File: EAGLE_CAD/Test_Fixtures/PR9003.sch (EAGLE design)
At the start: 2 parts, among them J1 AVR_SPI_PRG_6NS, J2 AVR_SPI_PRG_6NS

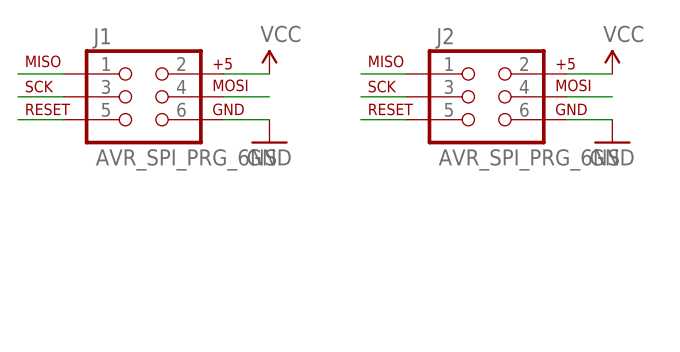
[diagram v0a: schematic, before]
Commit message: PR9003
Added external vcc line to programmer pcb
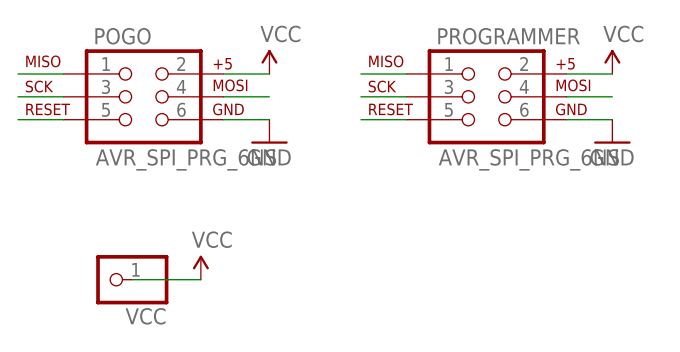
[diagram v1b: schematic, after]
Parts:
- added VCC: (no value), adafruit:PINHD-1X1
- renumbered J1 to POGO, J2 to PROGRAMMER
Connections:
- net VCC: now also VCC.1
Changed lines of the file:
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@@
 </classes>
 <parts>
-<part name="J1" library="SparkFun-Connectors" deviceset="AVR_SPI_PRG_6" device="NS"/>
-<part name="J2" library="SparkFun-Connectors" deviceset="AVR_SPI_PRG_6" device="NS"/>
+<part name="POGO" library="SparkFun-Connectors" deviceset="AVR_SPI_PRG_6" device="NS"/>
+<part name="PROGRAMMER" library="SparkFun-Connectors" deviceset="AVR_SPI_PRG_6" device="NS"/>
 <part name="GND1" library="SparkFun-Aesthetics" deviceset="GND" device=""/>
 <part name="GND2" library="SparkFun-Aesthetics" deviceset="GND" device=""/>
 <part name="SUPPLY1" library="SparkFun-Aesthetics" deviceset="VCC" device=""/>
 <part name="SUPPLY2" library="SparkFun-Aesthetics" deviceset="VCC" device=""/>
+<part name="VCC" library="adafruit" deviceset="PINHD-1X1" device=""/>
+<part name="SUPPLY3" library="SparkFun-Aesthetics" deviceset="VCC" device=""/>
 </parts>
 <sheets>
@@
 </plain>
 <instances>
-<instance part="J1" gate="G$1" x="20.32" y="17.78"/>
-<instance part="J2" gate="G$1" x="58.42" y="17.78"/>
+<instance part="POGO" gate="G$1" x="20.32" y="17.78"/>
+<instance part="PROGRAMMER" gate="G$1" x="58.42" y="17.78"/>
 <instance part="GND1" gate="1" x="35.56" y="12.7"/>
 <instance part="GND2" gate="1" x="73.66" y="12.7"/>
 <instance part="SUPPLY1" gate="G$1" x="35.56" y="20.32"/>
 <instance part="SUPPLY2" gate="G$1" x="73.66" y="20.32"/>
+<instance part="VCC" gate="G$1" x="17.78" y="-2.54" rot="R180"/>
+<instance part="SUPPLY3" gate="G$1" x="27.94" y="-2.54"/>
 </instances>
 <busses>
@@
 <net name="MISO" class="0">
 <segment>
-<pinref part="J1" gate="G$1" pin="1"/>
+<pinref part="POGO" gate="G$1" pin="1"/>
 <wire x1="12.7" y1="20.32" x2="7.62" y2="20.32" width="0.1524" layer="91"/>
 </segment>
 <segment>
-<pinref part="J2" gate="G$1" pin="1"/>
+<pinref part="PROGRAMMER" gate="G$1" pin="1"/>
 <wire x1="50.8" y1="20.32" x2="45.72" y2="20.32" width="0.1524" layer="91"/>
 </segment>
@@
 <net name="SCK" class="0">
 <segment>
-<pinref part="J1" gate="G$1" pin="3"/>
+<pinref part="POGO" gate="G$1" pin="3"/>
 <wire x1="12.7" y1="17.78" x2="7.62" y2="17.78" width="0.1524" layer="91"/>
 </segment>
 <segment>
-<pinref part="J2" gate="G$1" pin="3"/>
+<pinref part="PROGRAMMER" gate="G$1" pin="3"/>
 <wire x1="50.8" y1="17.78" x2="45.72" y2="17.78" width="0.1524" layer="91"/>
 </segment>
@@
 <net name="RESET" class="0">
 <segment>
-<pinref part="J1" gate="G$1" pin="5"/>
+<pinref part="POGO" gate="G$1" pin="5"/>
 <wire x1="12.7" y1="15.24" x2="7.62" y2="15.24" width="0.1524" layer="91"/>
 </segment>
 <segment>
-<pinref part="J2" gate="G$1" pin="5"/>
+<pinref part="PROGRAMMER" gate="G$1" pin="5"/>
 <wire x1="50.8" y1="15.24" x2="45.72" y2="15.24" width="0.1524" layer="91"/>
 </segment>
@@
 <net name="MOSI" class="0">
 <segment>
-<pinref part="J1" gate="G$1" pin="4"/>
+<pinref part="POGO" gate="G$1" pin="4"/>
 <wire x1="30.48" y1="17.78" x2="35.56" y2="17.78" width="0.1524" layer="91"/>
 </segment>
 <segment>
-<pinref part="J2" gate="G$1" pin="4"/>
+<pinref part="PROGRAMMER" gate="G$1" pin="4"/>
 <wire x1="68.58" y1="17.78" x2="73.66" y2="17.78" width="0.1524" layer="91"/>
 </segment>
@@
 <net name="GND" class="0">
 <segment>
-<pinref part="J1" gate="G$1" pin="6"/>
+<pinref part="POGO" gate="G$1" pin="6"/>
 <wire x1="30.48" y1="15.24" x2="35.56" y2="15.24" width="0.1524" layer="91"/>
 <pinref part="GND1" gate="1" pin="GND"/>
 </segment>
 <segment>
-<pinref part="J2" gate="G$1" pin="6"/>
+<pinref part="PROGRAMMER" gate="G$1" pin="6"/>
 <wire x1="68.58" y1="15.24" x2="73.66" y2="15.24" width="0.1524" layer="91"/>
 <pinref part="GND2" gate="1" pin="GND"/>
@@
 <net name="VCC" class="0">
 <segment>
-<pinref part="J1" gate="G$1" pin="2"/>
+<pinref part="POGO" gate="G$1" pin="2"/>
 <wire x1="30.48" y1="20.32" x2="35.56" y2="20.32" width="0.1524" layer="91"/>
 <pinref part="SUPPLY1" gate="G$1" pin="VCC"/>
 </segment>
 <segment>
-<pinref part="J2" gate="G$1" pin="2"/>
+<pinref part="PROGRAMMER" gate="G$1" pin="2"/>
 <wire x1="68.58" y1="20.32" x2="73.66" y2="20.32" width="0.1524" layer="91"/>
 <pinref part="SUPPLY2" gate="G$1" pin="VCC"/>
 </segment>
+<segment>
+<pinref part="VCC" gate="G$1" pin="1"/>
+<pinref part="SUPPLY3" gate="G$1" pin="VCC"/>
+<wire x1="27.94" y1="-2.54" x2="20.32" y2="-2.54" width="0.1524" layer="91"/>
+</segment>
 </net>

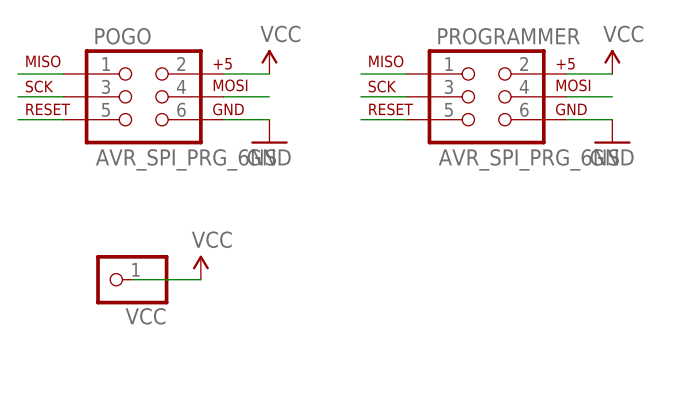
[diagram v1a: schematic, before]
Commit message: PR9003
Updated programmer w/ external vcc & gnd
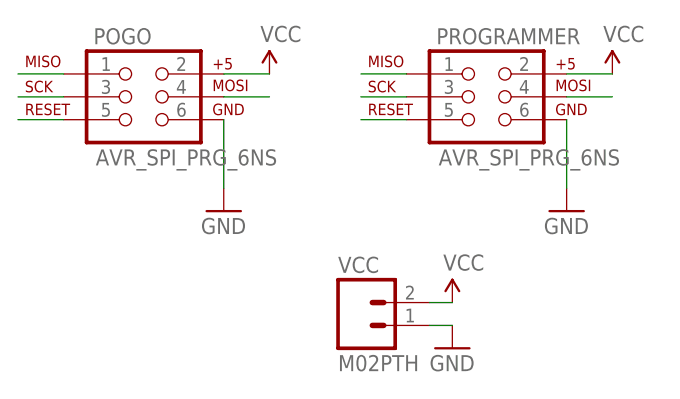
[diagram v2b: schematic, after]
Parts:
- VCC: value (none) -> M02PTH; device adafruit:PINHD-1X1 -> SparkFun-Connectors:M02PTH
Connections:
- net GND: now also VCC.1
- net VCC: now also VCC.2; no longer VCC.1
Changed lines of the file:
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@@
 <part name="SUPPLY1" library="SparkFun-Aesthetics" deviceset="VCC" device=""/>
 <part name="SUPPLY2" library="SparkFun-Aesthetics" deviceset="VCC" device=""/>
-<part name="VCC" library="adafruit" deviceset="PINHD-1X1" device=""/>
 <part name="SUPPLY3" library="SparkFun-Aesthetics" deviceset="VCC" device=""/>
+<part name="VCC" library="SparkFun-Connectors" deviceset="M02" device="PTH"/>
+<part name="GND3" library="SparkFun-Aesthetics" deviceset="GND" device=""/>
 </parts>
 <sheets>
@@
 <instance part="POGO" gate="G$1" x="20.32" y="17.78"/>
 <instance part="PROGRAMMER" gate="G$1" x="58.42" y="17.78"/>
-<instance part="GND1" gate="1" x="35.56" y="12.7"/>
-<instance part="GND2" gate="1" x="73.66" y="12.7"/>
+<instance part="GND1" gate="1" x="30.48" y="5.08"/>
+<instance part="GND2" gate="1" x="68.58" y="5.08"/>
 <instance part="SUPPLY1" gate="G$1" x="35.56" y="20.32"/>
 <instance part="SUPPLY2" gate="G$1" x="73.66" y="20.32"/>
-<instance part="VCC" gate="G$1" x="17.78" y="-2.54" rot="R180"/>
-<instance part="SUPPLY3" gate="G$1" x="27.94" y="-2.54"/>
+<instance part="SUPPLY3" gate="G$1" x="55.88" y="-5.08"/>
+<instance part="VCC" gate="G$1" x="45.72" y="-7.62"/>
+<instance part="GND3" gate="1" x="55.88" y="-10.16"/>
 </instances>
 <busses>
@@
 <segment>
 <pinref part="POGO" gate="G$1" pin="6"/>
-<wire x1="30.48" y1="15.24" x2="35.56" y2="15.24" width="0.1524" layer="91"/>
+<wire x1="30.48" y1="15.24" x2="30.48" y2="7.62" width="0.1524" layer="91"/>
 <pinref part="GND1" gate="1" pin="GND"/>
 </segment>
 <segment>
 <pinref part="PROGRAMMER" gate="G$1" pin="6"/>
-<wire x1="68.58" y1="15.24" x2="73.66" y2="15.24" width="0.1524" layer="91"/>
+<wire x1="68.58" y1="15.24" x2="68.58" y2="7.62" width="0.1524" layer="91"/>
 <pinref part="GND2" gate="1" pin="GND"/>
+</segment>
+<segment>
+<pinref part="VCC" gate="G$1" pin="1"/>
+<pinref part="GND3" gate="1" pin="GND"/>
+<wire x1="55.88" y1="-7.62" x2="53.34" y2="-7.62" width="0.1524" layer="91"/>
 </segment>
 </net>
@@
 </segment>
 <segment>
-<pinref part="VCC" gate="G$1" pin="1"/>
+<pinref part="VCC" gate="G$1" pin="2"/>
 <pinref part="SUPPLY3" gate="G$1" pin="VCC"/>
-<wire x1="27.94" y1="-2.54" x2="20.32" y2="-2.54" width="0.1524" layer="91"/>
+<wire x1="55.88" y1="-5.08" x2="53.34" y2="-5.08" width="0.1524" layer="91"/>
 </segment>
 </net>

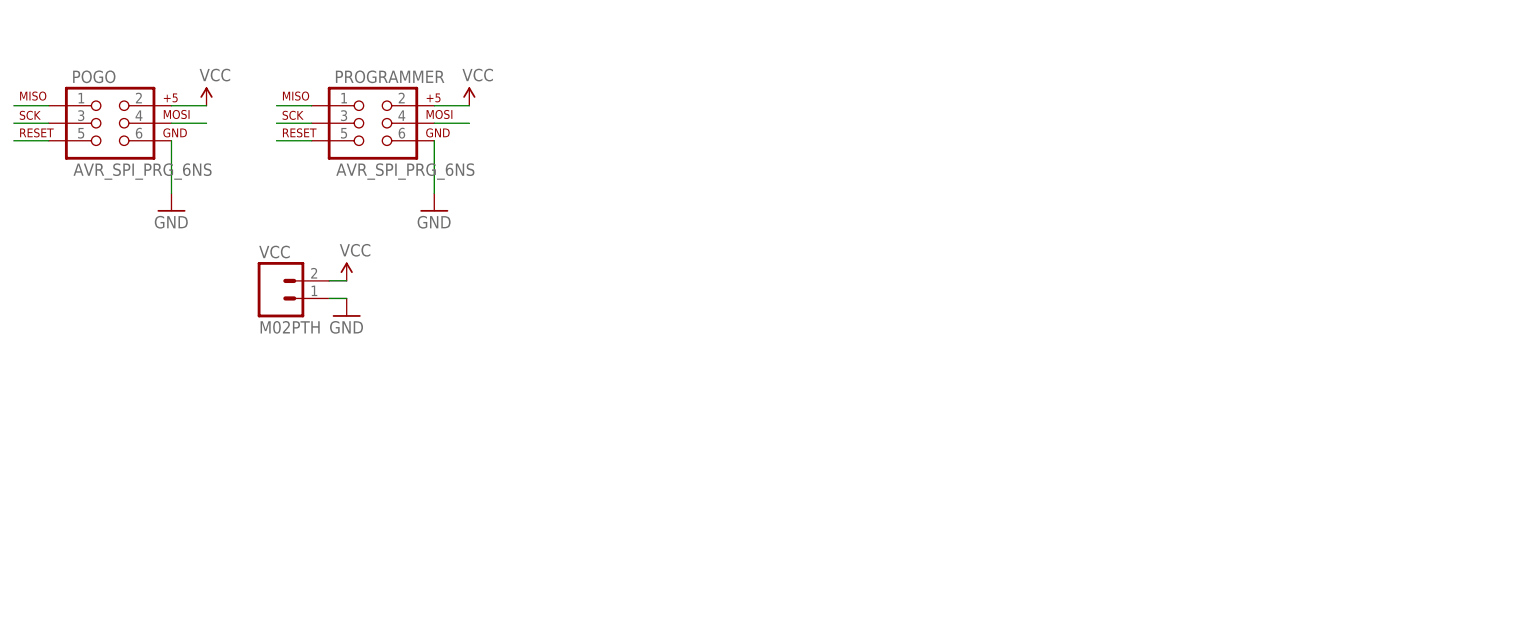
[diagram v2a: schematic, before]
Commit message: 9003 updates
added test points for all locations
rerouted vcc so DUT can only be programed when the POT is in the on position.

to do:
route traces
add package for push button
add push button
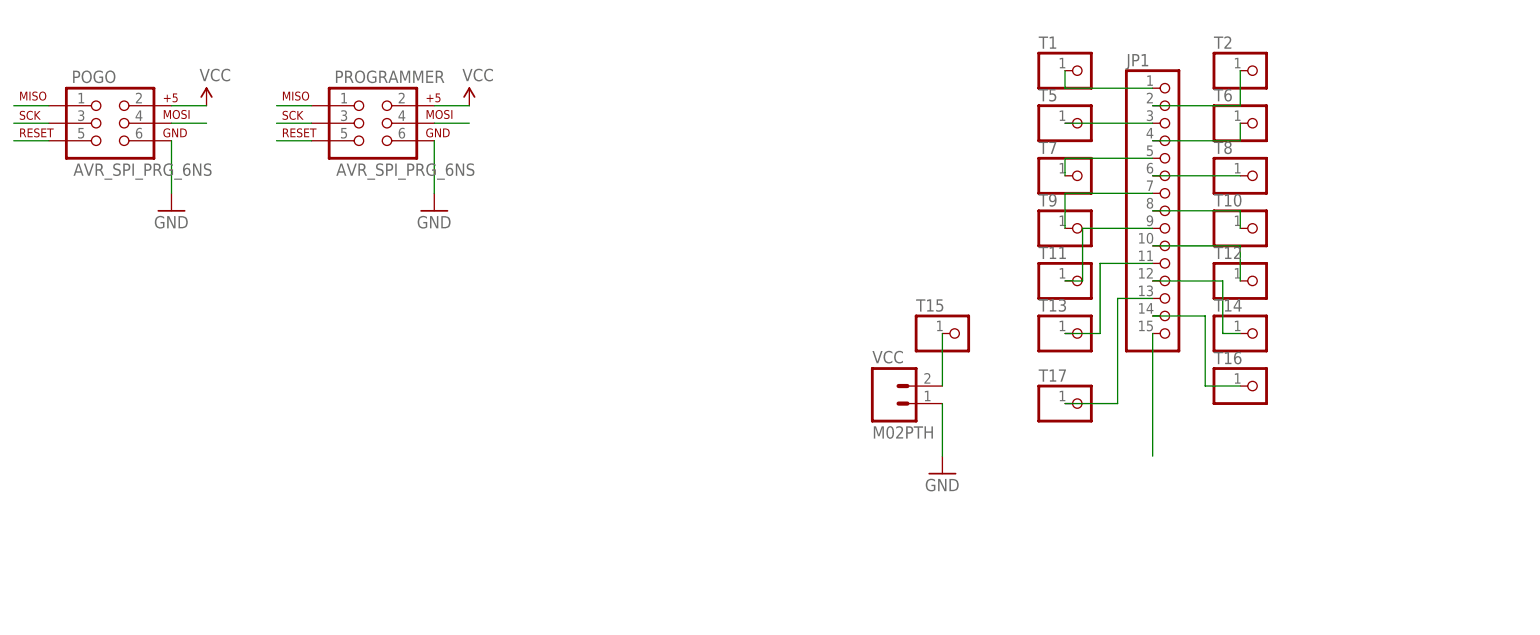
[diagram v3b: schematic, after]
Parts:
- added JP1: (no value), adafruit:PINHD-1X15
- added T1, T10, T11, T12, T13, T14, T15, T16, T17, T2, T5, T6, T7, T8, T9: (no value), adafruit:PINHD-1X1
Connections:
- new net N$1: JP1.1, T1.1
- new net N$10: JP1.10, T12.1
- new net N$11: JP1.11, T13.1
- new net N$12: JP1.12, T14.1
- new net N$13: T15.1, VCC.2
- new net N$14: JP1.14, T16.1
- new net N$15: JP1.13, T17.1
- new net N$16: JP1.15
- new net N$2: JP1.2, T2.1
- new net N$3: JP1.3, T5.1
- new net N$4: JP1.4, T6.1
- new net N$5: JP1.5, T7.1
- new net N$6: JP1.6, T8.1
- new net N$7: JP1.7, T9.1
- new net N$8: JP1.8, T10.1
- new net N$9: JP1.9, T11.1
- net VCC: no longer VCC.2
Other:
- moved on the sheet: VCC

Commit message: PR9003
Routed test point connections
Added push button to library and PCB (https://www.digikey.com/product-detail/en/c-k/D6C40-F2-LFS/401-1985-ND/1466342)

Push button is wired to be used with an RPI pin that should be set high with an internal pull up. Button press will trigger an active low state. Probably need to use the Wiring PiC library.  This will reduce parts needed and eliminate the need to bring 3.3V to the test board.
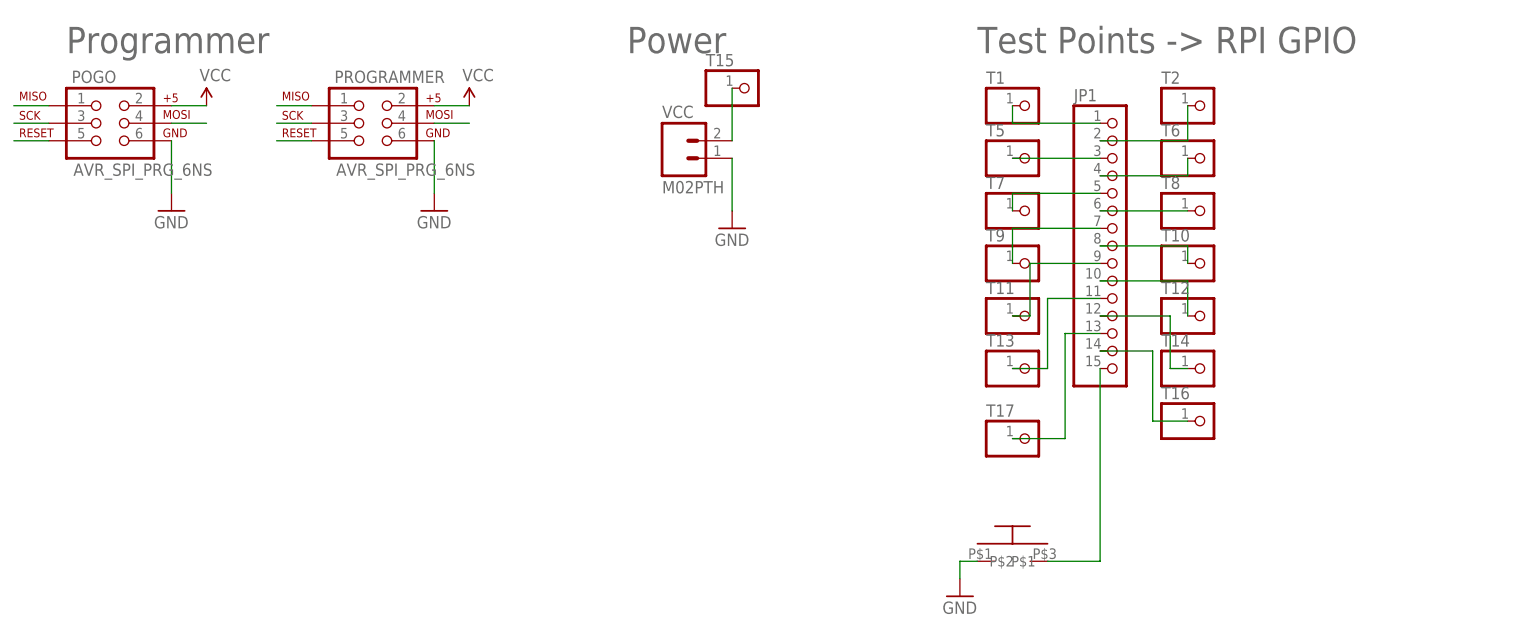
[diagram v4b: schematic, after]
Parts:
- added U$1: C&K_D6C_SWITCH, PR_Parts_Library:C&K_D6C_SWITCH
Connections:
- net GND: now also U$1.P$1
- net N$16: now also U$1.P$2
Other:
- note added: "Power"
- note added: "Programmer"
- note added: "Test Points -> RPI GPIO"
- moved on the sheet: JP1, T1, T10, T11, T12, T13, T14, T15, T16, T17, T2, T5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
